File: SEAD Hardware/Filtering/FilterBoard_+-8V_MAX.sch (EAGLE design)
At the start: 98 parts, among them U1 TLC2272A_D_8, U2 TLC2272A_D_8, U3 TLC2272A_D_8, U4 TLC2272A_D_8, U5 TLC2272A_D_8, U6 TLC2272A_D_8, U7 TPS7A3301_RGW_20, U8 TPS84250_RKG_41

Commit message: Finished new filter board prototype.
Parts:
- removed R18, R23: (no value), SensorCape:RESISTOR0805-RES
- added C44, C55, C56, C57, C58, C59, C60, C61, C62, C63, C64, C65: 10nF, SensorCape:CAP0805
- added LED1, LED2, LED3, LED4, LED5: (no value), ASL:LED1206
- added R28, R35, R36, R37, R38: (no value), ASL:RESISTOR0805-RES
- added R39: 0, ASL:RESISTOR1206
- added R40, R41: (no value), pot:TRIM_EU-B64Y
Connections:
- removed net HVSS_8D: U1G$2.V-, U2G$2.V-, U3G$2.V-, U4G$2.V-, U5G$2.V-, U6G$2.V-
- new net N$30: LED1.C, R28.2
- new net N$45: LED2.C, R35.2
- new net N$46: LED3.C, R36.2
- new net N$47: LED4.C, R37.2
- new net N$48: LED5.C, R38.2
- new net VDD_L_CHOKE: B1.AC2, R39.1
- net GND: now also C44.2, C55.2, C56.1, C57.2, C58.1, C59.2, C60.1, C61.2, C62.1, C63.1, C64.1, C65.2, R28.1, R35.1, R36.1, R37.1, R38.1, R39.2; no longer B1.AC2
- net HVDD_15D: now also LED1.A
- net HVDD_8A: now also C44.1, C56.2, C58.2, C60.2, C62.2, C64.2, LED4.A
- net HVDD_IN: now also LED5.A
- net HVSS_15D: now also LED2.A
- net HVSS_8A: now also C55.1, C57.1, C59.1, C61.1, C63.2, C65.1, LED3.A, U1G$2.V-, U2G$2.V-, U3G$2.V-, U4G$2.V-, U5G$2.V-, U6G$2.V-
- net N$19: now also R40.S; no longer R18.1
- net N$22: now also R41.E; no longer R23.1
- net OUT_15KHZ: now also R41.S; no longer R23.2
- net OUT_15_100_KHZ: now also R40.A; no longer R18.2

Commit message: Fixed -V switcher on filtering board.
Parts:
- removed C44, C55, C56, C57, C62, C63: 10nF, SensorCape:CAP0805
- removed R40, R41: (no value), pot:TRIM_EU-B64Y
- removed U1, U2, U3, U4, U5, U6: TLC2272A_D_8, SensorCape:TLC2272A_D_8
- added IC1, IC2, IC3: TL084D, linear:TL084D
- added R18, R23: (no value), pot:TRIM_EU-B90P
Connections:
- removed net N$11: U4G$1.-IN, U4G$1.OUT
- net GND: now also U$2.0P8V, U$2.3P2V; no longer C44.2, C55.2, C56.1, C57.2, C62.1, C63.1, U$1.A_VOUT, U$1.VOUT_PT
- net HVDD_8A: now also IC1P.V+, IC2P.V+, IC3P.V+; no longer C44.1, C56.2, C62.2, U1G$2.V+, U2G$2.V+, U3G$2.V+, U4G$2.V+, U5G$2.V+, U6G$2.V+
- net HVSS_15D: now also U$1.A_VOUT, U$1.VOUT_PT
- net HVSS_8A: now also IC1P.V-, IC2P.V-, IC3P.V-; no longer C55.1, C57.1, C63.2, U1G$2.V-, U2G$2.V-, U3G$2.V-, U4G$2.V-, U5G$2.V-, U6G$2.V-
- net N$10: now also IC2D.+IN; no longer U4G$2.+IN
- net N$12: now also IC1A.-IN, IC1A.OUT; no longer U1G$1.-IN, U1G$1.OUT
- net N$14: now also IC1B.+IN; no longer U1G$2.+IN
- net N$15: now also IC1B.-IN, IC1B.OUT; no longer U1G$2.-IN, U1G$2.OUT
- net N$16: now also IC1C.-IN, IC1C.OUT; no longer U2G$1.-IN, U2G$1.OUT
- net N$17: now also IC1D.-IN, IC1D.OUT; no longer U2G$2.-IN, U2G$2.OUT
- net N$18: now also IC2A.-IN, IC2A.OUT; no longer U3G$1.-IN, U3G$1.OUT
- net N$19: now also IC2B.-IN, R18.S; no longer R40.S, U3G$2.-IN
- net N$20: now also IC3C.+IN; no longer U6G$1.+IN
- net N$21: now also IC3D.+IN; no longer U6G$2.+IN
- net N$22: now also IC3D.-IN, R23.S; no longer R41.E, U6G$2.-IN
- net N$24: now also IC3B.-IN, IC3B.OUT; no longer U5G$2.-IN, U5G$2.OUT
- net N$26: now also IC3B.+IN; no longer U5G$2.+IN
- net N$28: now also IC3A.-IN, IC3A.OUT; no longer U5G$1.-IN, U5G$1.OUT
- net N$29: now also IC3A.+IN; no longer U5G$1.+IN
- net N$3: now also IC2C.-IN, IC2C.OUT
- net N$31: now also IC2D.-IN, IC2D.OUT; no longer U4G$2.-IN, U4G$2.OUT
- net N$36: now also IC1C.+IN; no longer U2G$1.+IN
- net N$38: now also IC1D.+IN; no longer U2G$2.+IN
- net N$4: now also IC3C.-IN, IC3C.OUT; no longer U6G$1.-IN, U6G$1.OUT
- net N$41: now also IC2A.+IN; no longer U3G$1.+IN
- net N$42: now also IC2B.+IN; no longer U3G$2.+IN
- net N$7: now also IC1A.+IN, IC2C.+IN; no longer U1G$1.+IN, U4G$1.+IN
- net OUT_15KHZ: now also IC3D.OUT, R23.E; no longer R41.S, U6G$2.OUT
- net OUT_15_100_KHZ: now also IC2B.OUT, R18.E; no longer R40.A, U3G$2.OUT

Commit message: Filtering Circuit v1.6
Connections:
- net GND: no longer C46.2, U$1.RT
- net HVSS_15D: now also C46.2, U$1.RT, U$1.STSEL
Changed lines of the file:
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@@
 <pinref part="R30" gate="G$1" pin="1"/>
 <wire x1="485.14" y1="116.84" x2="485.14" y2="66.04" width="0.1524" layer="91"/>
-<wire x1="485.14" y1="66.04" x2="492.76" y2="66.04" width="0.1524" layer="91"/>
-<wire x1="492.76" y1="66.04" x2="543.56" y2="66.04" width="0.1524" layer="91"/>
-<wire x1="543.56" y1="66.04" x2="581.66" y2="66.04" width="0.1524" layer="91"/>
-<pinref part="C46" gate="G$1" pin="2"/>
-<wire x1="492.76" y1="73.66" x2="492.76" y2="66.04" width="0.1524" layer="91"/>
-<junction x="492.76" y="66.04"/>
-<junction x="543.56" y="66.04"/>
+<wire x1="485.14" y1="66.04" x2="581.66" y2="66.04" width="0.1524" layer="91"/>
 <pinref part="U$1" gate="A" pin="GND"/>
 <wire x1="533.4" y1="119.38" x2="543.56" y2="119.38" width="0.1524" layer="91"/>
@@
 <wire x1="581.66" y1="66.04" x2="581.66" y2="119.38" width="0.1524" layer="91"/>
 <junction x="581.66" y="119.38"/>
-<pinref part="U$1" gate="A" pin="RT"/>
-<wire x1="533.4" y1="81.28" x2="543.56" y2="81.28" width="0.1524" layer="91"/>
-<wire x1="543.56" y1="81.28" x2="543.56" y2="66.04" width="0.1524" layer="91"/>
 </segment>
 <segment>
@@
 <wire x1="518.16" y1="73.66" x2="518.16" y2="71.12" width="0.1524" layer="91"/>
 <label x="515.62" y="71.12" size="1.778" layer="95"/>
-</segment>
-</net>
+<pinref part="U$1" gate="A" pin="STSEL"/>
+<wire x1="502.92" y1="81.28" x2="502.92" y2="73.66" width="0.1524" layer="91"/>
+<wire x1="502.92" y1="73.66" x2="518.16" y2="73.66" width="0.1524" layer="91"/>
+<pinref part="U$1" gate="A" pin="RT"/>
+<wire x1="533.4" y1="81.28" x2="543.56" y2="81.28" width="0.1524" layer="91"/>
+<wire x1="543.56" y1="81.28" x2="543.56" y2="73.66" width="0.1524" layer="91"/>
+<wire x1="543.56" y1="73.66" x2="518.16" y2="73.66" width="0.1524" layer="91"/>
+<pinref part="C46" gate="G$1" pin="2"/>
+<wire x1="492.76" y1="73.66" x2="502.92" y2="73.66" width="0.1524" layer="91"/>
+</segment>
+</net>

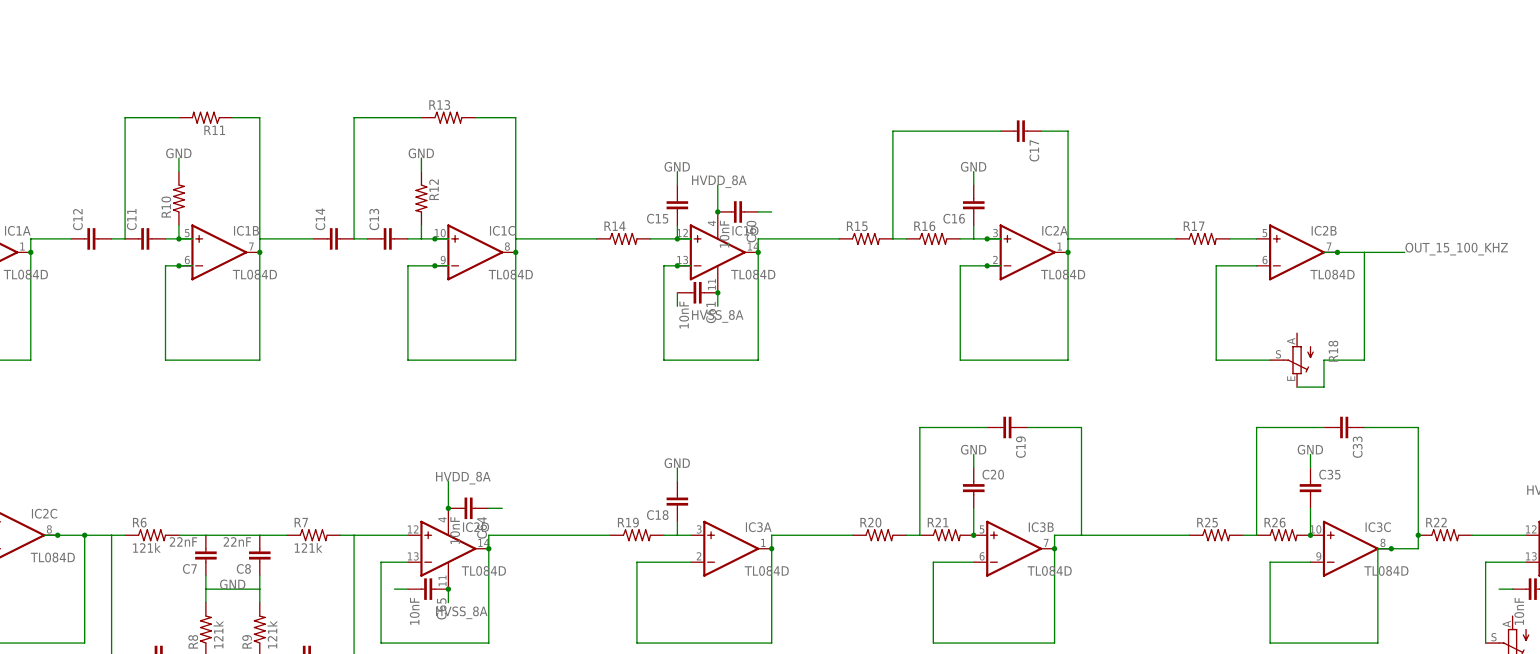
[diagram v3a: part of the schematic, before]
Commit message: DAQ and BBB now talking and capturing data
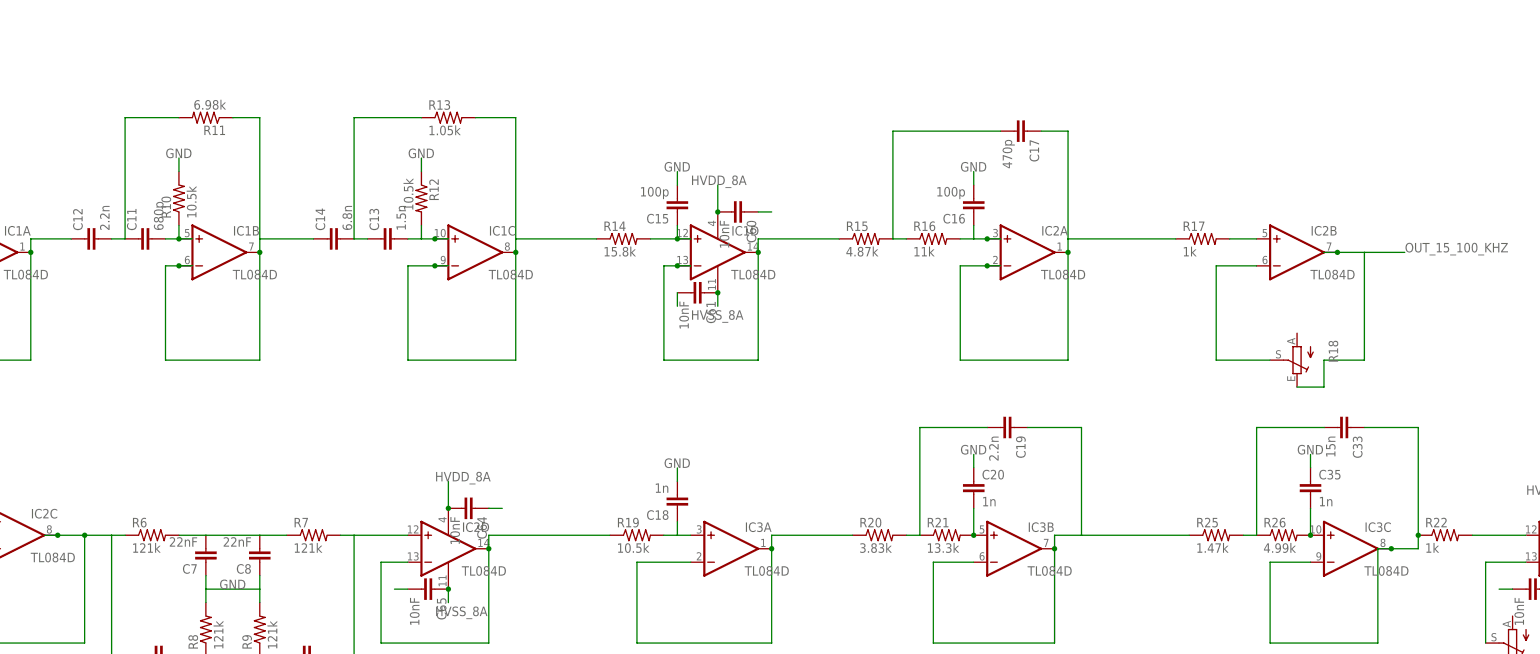
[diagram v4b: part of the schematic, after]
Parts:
- C11: value (none) -> 680p
- C12, C19: value (none) -> 2.2n
- C13: value (none) -> 1.5n
- C14: value (none) -> 6.8n
- C15, C16: value (none) -> 100p
- C17: value (none) -> 470p
- C18, C20, C35: value (none) -> 1n
- C33: value (none) -> 15n
- R10, R12, R19: value (none) -> 10.5k
- R11: value (none) -> 6.98k
- R13: value (none) -> 1.05k
- R14: value (none) -> 15.8k
- R15: value (none) -> 4.87k
- R16: value (none) -> 11k
- R17, R22: value (none) -> 1k
- R20: value (none) -> 3.83k
- R21: value (none) -> 13.3k
- R25: value (none) -> 1.47k
- R26: value (none) -> 4.99k
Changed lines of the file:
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@@
 <part name="R8" library="SensorCape" deviceset="RESISTOR" device="0805-RES" value="121k"/>
 <part name="R9" library="SensorCape" deviceset="RESISTOR" device="0805-RES" value="121k"/>
-<part name="C11" library="SensorCape" deviceset="CAP" device="1206"/>
-<part name="C12" library="SensorCape" deviceset="CAP" device="1206"/>
-<part name="C13" library="SensorCape" deviceset="CAP" device="1206"/>
-<part name="C14" library="SensorCape" deviceset="CAP" device="1206"/>
-<part name="C15" library="SensorCape" deviceset="CAP" device="1206"/>
-<part name="C16" library="SensorCape" deviceset="CAP" device="1206"/>
-<part name="C17" library="SensorCape" deviceset="CAP" device="1206"/>
-<part name="R10" library="SensorCape" deviceset="RESISTOR" device="0805-RES"/>
-<part name="R11" library="SensorCape" deviceset="RESISTOR" device="0805-RES"/>
-<part name="R12" library="SensorCape" deviceset="RESISTOR" device="0805-RES"/>
-<part name="R13" library="SensorCape" deviceset="RESISTOR" device="0805-RES"/>
-<part name="R14" library="SensorCape" deviceset="RESISTOR" device="0805-RES"/>
-<part name="R15" library="SensorCape" deviceset="RESISTOR" device="0805-RES"/>
-<part name="R16" library="SensorCape" deviceset="RESISTOR" device="0805-RES"/>
-<part name="R17" library="SensorCape" deviceset="RESISTOR" device="0805-RES"/>
-<part name="R19" library="SensorCape" deviceset="RESISTOR" device="0805-RES"/>
-<part name="C18" library="SensorCape" deviceset="CAP" device="1206"/>
-<part name="R20" library="SensorCape" deviceset="RESISTOR" device="0805-RES"/>
-<part name="R21" library="SensorCape" deviceset="RESISTOR" device="0805-RES"/>
-<part name="C19" library="SensorCape" deviceset="CAP" device="1206"/>
-<part name="C20" library="SensorCape" deviceset="CAP" device="1206"/>
-<part name="R22" library="SensorCape" deviceset="RESISTOR" device="0805-RES"/>
+<part name="C11" library="SensorCape" deviceset="CAP" device="1206" value="680p"/>
+<part name="C12" library="SensorCape" deviceset="CAP" device="1206" value="2.2n"/>
+<part name="C13" library="SensorCape" deviceset="CAP" device="1206" value="1.5n"/>
+<part name="C14" library="SensorCape" deviceset="CAP" device="1206" value="6.8n"/>
+<part name="C15" library="SensorCape" deviceset="CAP" device="1206" value="100p"/>
+<part name="C16" library="SensorCape" deviceset="CAP" device="1206" value="100p"/>
+<part name="C17" library="SensorCape" deviceset="CAP" device="1206" value="470p"/>
+<part name="R10" library="SensorCape" deviceset="RESISTOR" device="0805-RES" value="10.5k"/>
+<part name="R11" library="SensorCape" deviceset="RESISTOR" device="0805-RES" value="6.98k"/>
+<part name="R12" library="SensorCape" deviceset="RESISTOR" device="0805-RES" value="10.5k"/>
+<part name="R13" library="SensorCape" deviceset="RESISTOR" device="0805-RES" value="1.05k"/>
+<part name="R14" library="SensorCape" deviceset="RESISTOR" device="0805-RES" value="15.8k"/>
+<part name="R15" library="SensorCape" deviceset="RESISTOR" device="0805-RES" value="4.87k"/>
+<part name="R16" library="SensorCape" deviceset="RESISTOR" device="0805-RES" value="11k"/>
+<part name="R17" library="SensorCape" deviceset="RESISTOR" device="0805-RES" value="1k"/>
+<part name="R19" library="SensorCape" deviceset="RESISTOR" device="0805-RES" value="10.5k"/>
+<part name="C18" library="SensorCape" deviceset="CAP" device="1206" value="1n"/>
+<part name="R20" library="SensorCape" deviceset="RESISTOR" device="0805-RES" value="3.83k"/>
+<part name="R21" library="SensorCape" deviceset="RESISTOR" device="0805-RES" value="13.3k"/>
+<part name="C19" library="SensorCape" deviceset="CAP" device="1206" value="2.2n"/>
+<part name="C20" library="SensorCape" deviceset="CAP" device="1206" value="1n"/>
+<part name="R22" library="SensorCape" deviceset="RESISTOR" device="0805-RES" value="1k"/>
 <part name="JP1" library="ASL" deviceset="M03" device="-SCREW-5MM"/>
 <part name="U7" library="SensorCape" deviceset="TPS7A3301_RGW_20" device=""/>
@@
 <part name="C32" library="ASL" deviceset="CAP" device="0805" value="10uF"/>
 <part name="C34" library="SensorCape" deviceset="CAP" device="1206" value="10uF"/>
-<part name="R25" library="SensorCape" deviceset="RESISTOR" device="0805-RES"/>
-<part name="R26" library="SensorCape" deviceset="RESISTOR" device="0805-RES"/>
-<part name="C33" library="SensorCape" deviceset="CAP" device="1206"/>
-<part name="C35" library="SensorCape" deviceset="CAP" device="1206"/>
+<part name="R25" library="SensorCape" deviceset="RESISTOR" device="0805-RES" value="1.47k"/>
+<part name="R26" library="SensorCape" deviceset="RESISTOR" device="0805-RES" value="4.99k"/>
+<part name="C33" library="SensorCape" deviceset="CAP" device="1206" value="15n"/>
+<part name="C35" library="SensorCape" deviceset="CAP" device="1206" value="1n"/>
 <part name="C36" library="SensorCape" deviceset="CAP_POL" device="PTH3"/>
 <part name="C37" library="SensorCape" deviceset="CAP_POL" device="PTH3"/>
